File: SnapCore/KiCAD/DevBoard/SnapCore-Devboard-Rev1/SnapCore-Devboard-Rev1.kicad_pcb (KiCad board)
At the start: 4 copper layers, 26.8 x 49.4 mm, 56 parts, among them J2 USB_C_Receptacle_USB2.0_16P, J3 Conn_01x18_Pin, Q1 AO3407A, U1 nRF52840-QIXX, U2 XC6220B331MR, U5 TP4056-42-ESOP8, Y1 32.768KHz, Y2 32MHz

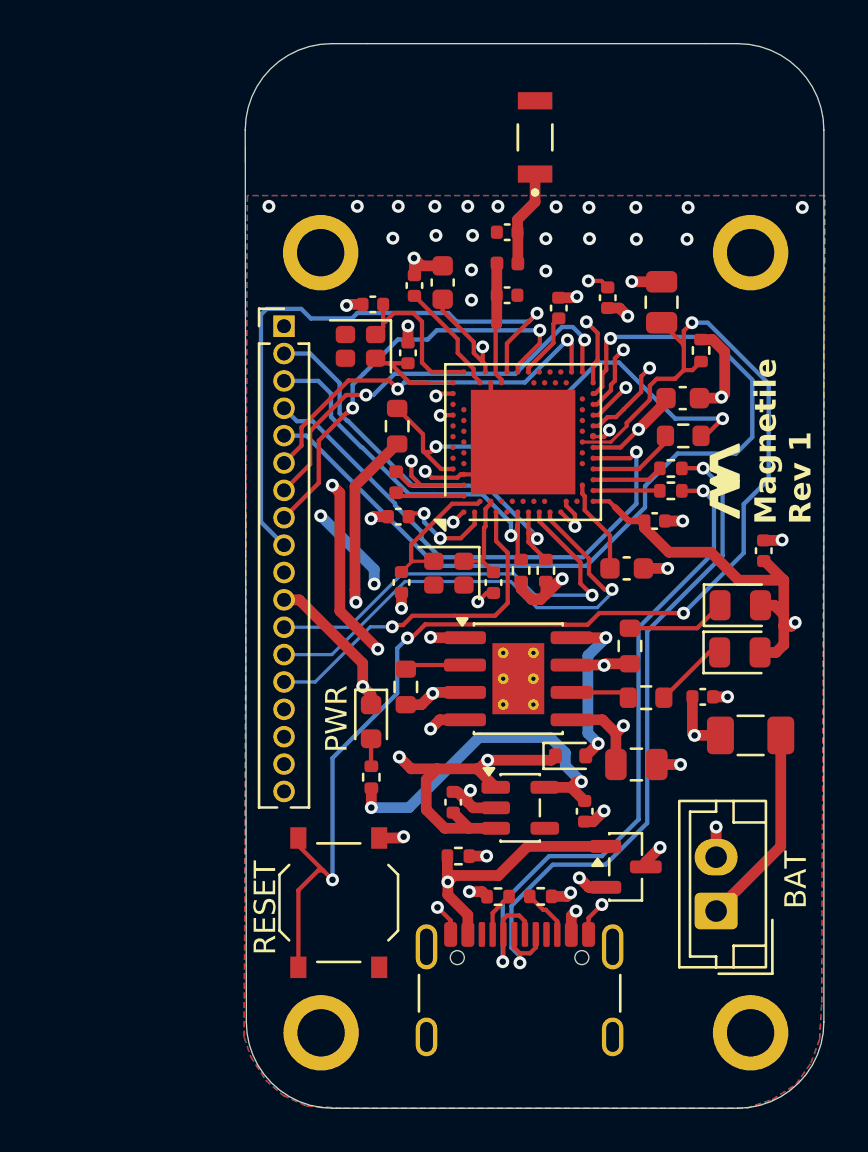
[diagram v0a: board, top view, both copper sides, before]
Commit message: Tried implementing AS5600 on the board
Added schematic
Need to rework layout first to integrate properly (or use breakout board instead)
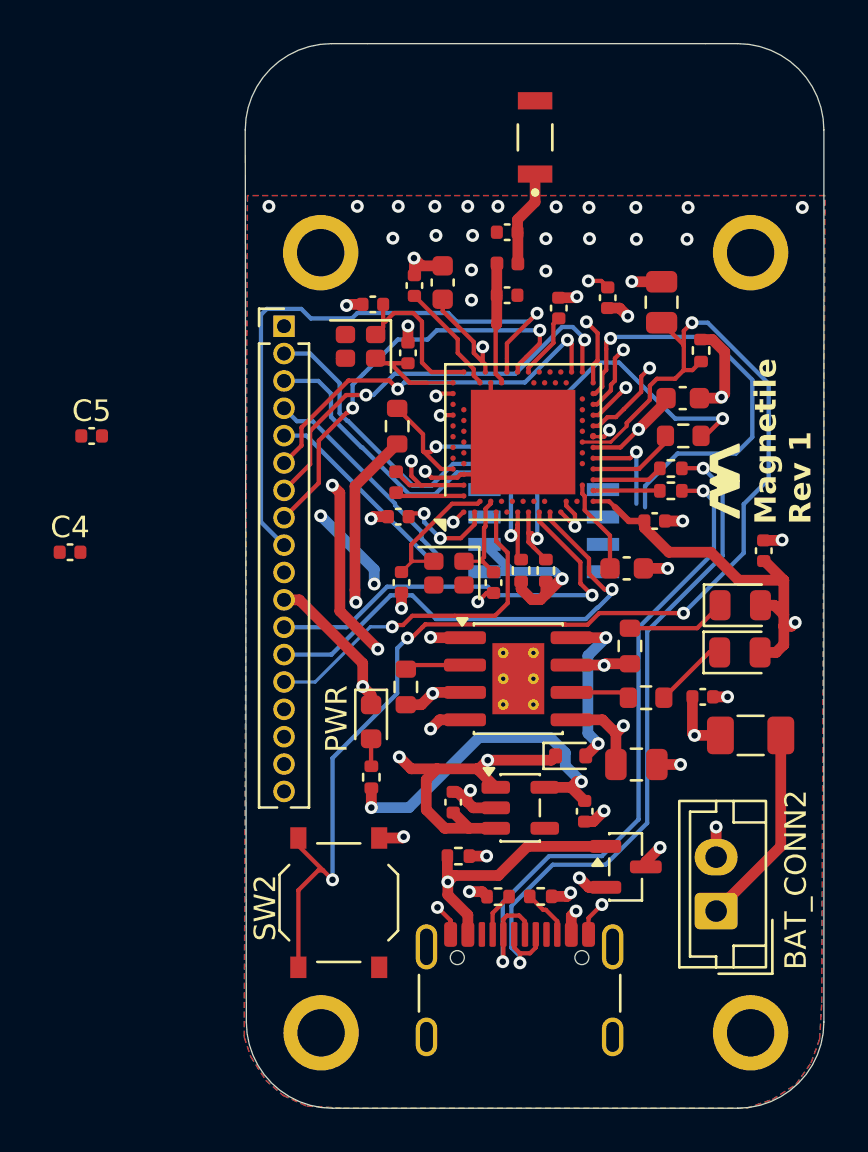
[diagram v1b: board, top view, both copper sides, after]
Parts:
- added C4: 100nF, Capacitor_SMD:C_0402_1005Metric, F.Cu at (90.1, 105.7)
- added C5: 10pF, Capacitor_SMD:C_0402_1005Metric, F.Cu at (91.1, 100.3)
- added U3: AS5600, AS5600:SOIC8, B.Cu at (112.1, 104.7)
- renumbered BAT to BAT_CONN2, RESET to SW2
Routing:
- net P1.00_PDM_CLK: track 40.3 -> 29.5 mm
- net P0.16_PDM_DATA: track 25.0 -> 14.9 mm
- net 3V3: track 98.8 -> 106.3 mm
- net INTERNAL_I2C_SDA: track 19.2 -> 21.8 mm
- net INTERNAL_I2C_SCL: track 17.4 -> 19.4 mm
